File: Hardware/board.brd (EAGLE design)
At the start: 106.4 x 75.2 mm, 105 parts, among them IC1 BQ25180YBGR, IC2 DRV2605YZFR, IC3 BMA423, IC9 RT6160AWSC, J1 503480-2400, J2 TC2030-IDC_TC2030-IDC, J4 KH-TYPE-C-16P, Q1 SI1308EDL-T1-GE3, Q2 3.1A/30V/105mΩ, U1 NRF52840_QF, U3 MAX17048G+T10, X1 32MHz, X2 32.768kHz

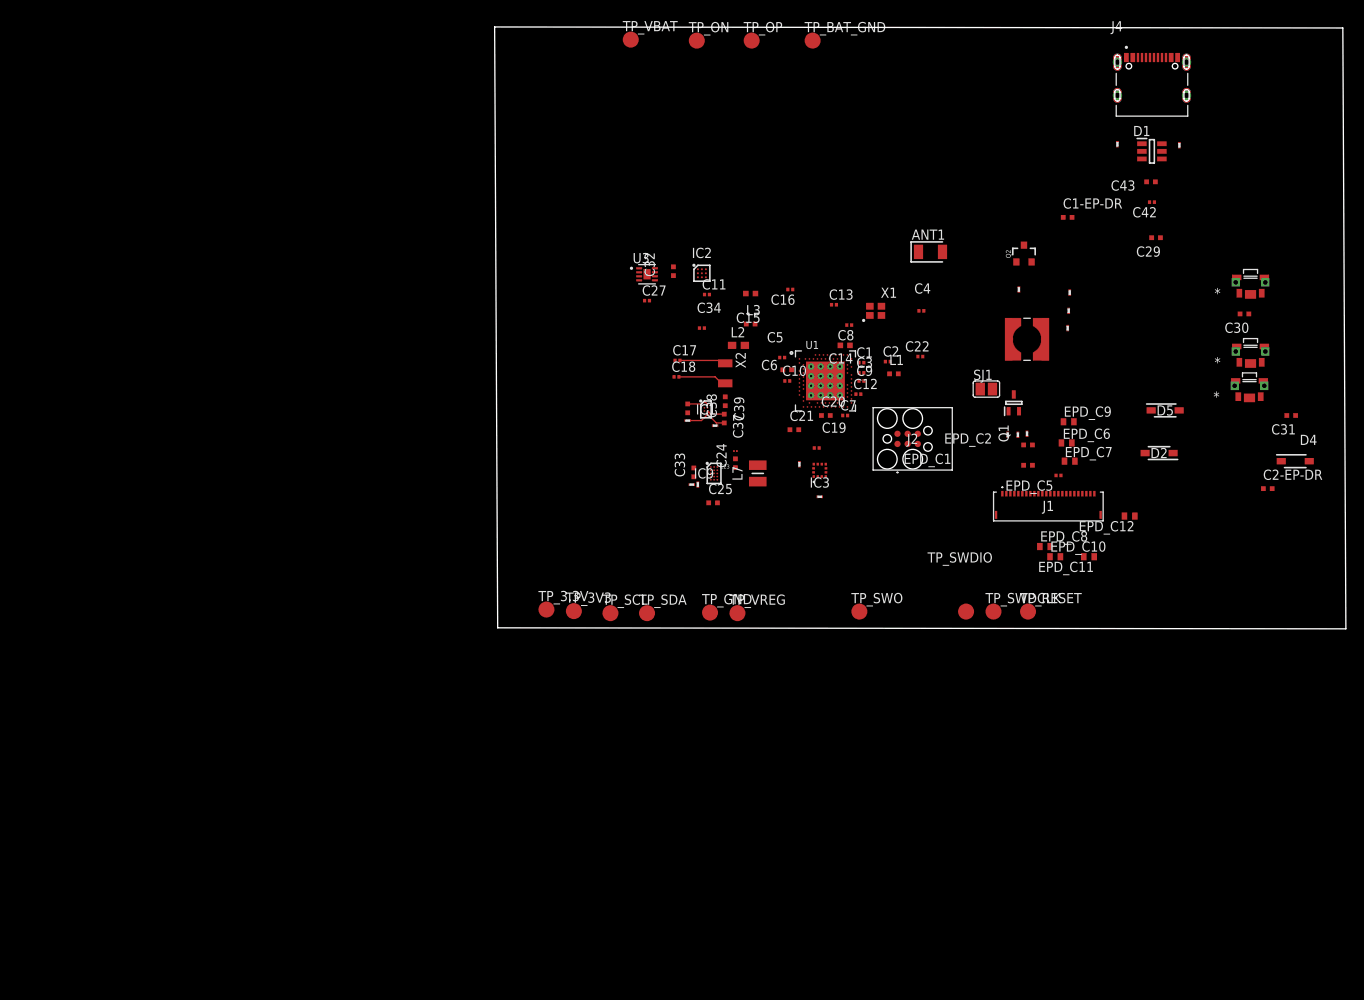
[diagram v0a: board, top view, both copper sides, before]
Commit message: Schematic and 2D PCB updated to final version
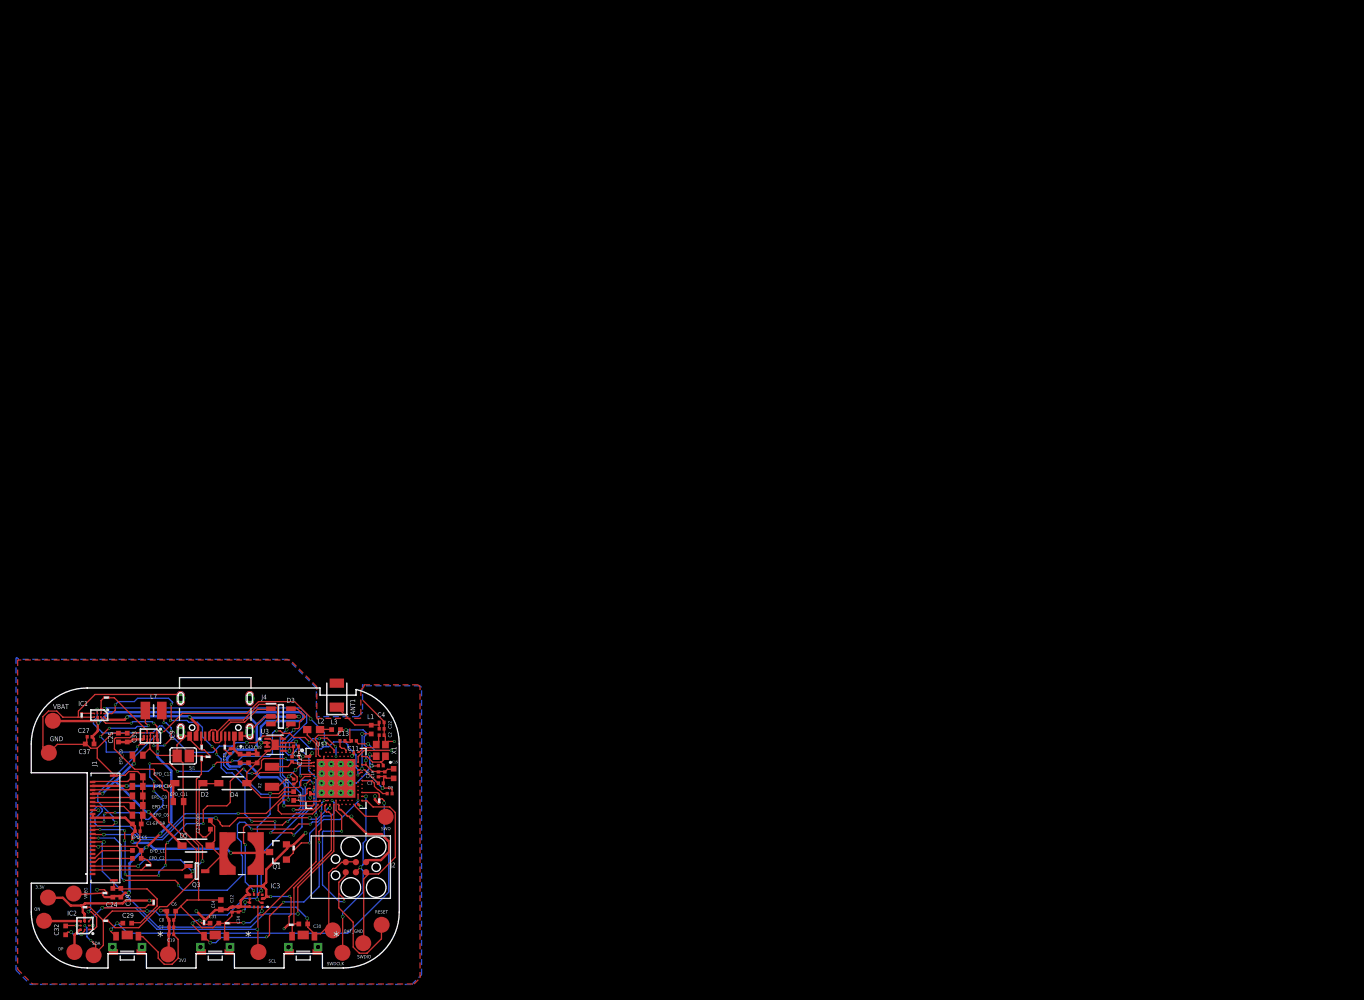
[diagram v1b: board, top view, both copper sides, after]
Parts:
- removed D1: ESP32_C6_LIBRARY_3_USBLC6-2SC6Y, InkTime_v5:ESP32_C6_LIBRARY_3_SOT95P280X145-6N
- removed Q2: 3.1A/30V/105mΩ, InkTime_v5:ESP32_C6_LIBRARY_4_ESP32_C6_LIBRARY_4_ESP32_C6_LIBRARY_4_ESP32_C6_LIBRARY_4_ESP32_WROVER_SPARKFUN-DISCRETESE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
- removed TP_3.3V, TP_3V3, TP_BAT_GND, TP_GND, TP_ON, TP_OP, TP_RESET, TP_SCL, TP_SDA, TP_SWDCLK, TP_SWDIO, TP_SWO, TP_VBAT, TP_VREG: HECTOR_WATCH_1_TPTP20R, InkTime_v5:HECTOR_WATCH_1_TP20R
- removed U1: NRF52840_QF, InkTime_v5:NORDIC_NRF_4_AQFN50P700X700X85_HS-74N
- added 3.3V, 3V3, BAT_GND, GND, ON, OP, RESET, SCL, SDA, SWDCLK, SWDIO, SWO, VBAT, VREG: HECTOR_WATCH_1_TPTP20R, InkTime_v5:HECTOR_WATCH_1_TP20R
- added D3: ESP32_C6_LIBRARY_3_USBLC6-2SC6Y, InkTime_v5:ESP32_C6_LIBRARY_3_SOT95P280X145-6N
- added Q3: SI1308EDL-T1-GE3, InkTime_v5:ESP32_C6_LIBRARY_6_SOT65P210X110-3N
- added U$1: NORDIC_NRF_4_NRF52840_QF, InkTime_v5:NORDIC_NRF_4_AQFN50P700X700X85_HS-74N
- C23: device InkTime_v5:GRM011R60J152KE01L_2_CAPC0201X13N -> InkTime_v5:GRM011R60J152KE01L_1_0201
- Q1: value SI1308EDL-T1-GE3 -> 3.1A/30V/105mΩ; device InkTime_v5:ESP32_C6_LIBRARY_6_SOT65P210X110-3N -> InkTime_v5:ESP32_C6_LIBRARY_4_ESP32_C6_LIBRARY_4_ESP32_C6_LIBRARY_4_ESP32_C6_LIBRARY_4_ESP32_WROVER_SPARKFUN-DISCRETESE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
- moved SW_DN 162.8 mm to (-11.0, -14.5), turned to 180 degrees
- moved C29 154.5 mm to (-11.0, -11.9), turned to 0 degrees
- moved C31 148.8 mm to (-0.10, -11.9), turned to 0 degrees
- moved SW_ENT 146.7 mm to (0.00, -14.5), turned to 180 degrees
- moved R2_USB 143.5 mm to (-1.70, 10.1)
- moved C30 140.2 mm to (11.0, -12.0), turned to 0 degrees
- moved SW_UP 139.5 mm to (11.0, -14.5), turned to 180 degrees
- moved J4 139.3 mm to (0.00, 16.2), turned to 180 degrees
- moved C1-EP-DR 138.9 mm to (-9.80, 0.50)
- moved D4 138.8 mm to (2.20, 5.60), turned to 180 degrees
- moved C2-EP-DR 138.7 mm to (-0.60, 0.40), turned to 90 degrees
- moved R1_USB 134.6 mm to (1.20, 10.1), turned to 180 degrees
- moved C42 134.1 mm to (1.90, 9.60), turned to 270 degrees
- moved C43 133.9 mm to (4.17, 8.70), turned to 270 degrees
- moved D5 132.8 mm to (-2.40, -2.20)
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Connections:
- net N$9 renamed 3.3V
- removed net 3V3/1.7D: C34.1, IC2.C2, Q2.2, R5.2, R7.2, R8.2, R_PWR_EPD.2
- removed net 3V3/2.4A: C12.1, C14.1, C19.1, C6.1, C7.1, C8.1, IC3.10, IC3.3, IC3.7, J2.1, R17.1, R18.1, TP_3.3V.TP, TP_3V3.TP, U1.P$A22, U1.P$AD14, U1.P$AD23, U1.P$B1, U1.P$W1, U1.P$Y2
- removed net ALERT/1.6C: U3.5
- removed net ALERT/2.5C: U1.P$J24
- removed net D+/1.5D: D1.4
- removed net D+/2.7D: U1.P$AD6
- removed net D-/1.5D: D1.6
- removed net D-/2.7D: U1.P$AD4
- removed net EPD_BUSY/1.5D: J1.9
- removed net EPD_BUSY/2.2D: U1.P$AD12
- removed net EPD_CS/1.4C: J1.12
- removed net EPD_CS/2.2D: U1.P$K2
- removed net EPD_DC/1.5D: J1.11
- removed net EPD_DC/2.2D: U1.P$AD10
- removed net EPD_RST/1.5D: J1.10
- removed net EPD_RST/2.2D: U1.P$AC11
- removed net HAPTIC_EN/1.4C: IC2.A1
- removed net HAPTIC_EN/2.6A: U1.P$U1
- removed net MOSI/1.5B: J1.14
- removed net MOSI/2.2D: U1.P$B13
- removed net P0.13/1.5D: C30.1, R5.1, SW_UP.2
- removed net P0.13/2.6C: U1.P$AD8
- removed net P0.14/1.5D: C31.1, R8.1, SW_ENT.2
- removed net P0.14/2.7C: U1.P$AC9
- removed net P1.01/1.6C: Q2.1, R_PWR_EPD.1
- removed net P1.01/2.4B: U1.P$Y23
- removed net P1.02/1.6C: C29.1, R7.1, SW_DN.2
- removed net P1.02/2.8C: U1.P$W24
- removed net SCK/1.5B: J1.13
- removed net SCK/2.2D: U1.P$A12
- removed net SCL/1.4C: IC2.C1, U3.7
- removed net SCL/2.4C: IC1.B1, IC3.12, R17.2, R4.1, TP_SCL.TP, U1.P$M2
- removed net SDA/1.4C: IC2.B2, U3.8
- removed net SDA/2.4C: IC1.C1, IC3.2, R1.1, R18.2, TP_SDA.TP, U1.P$L1
- removed net VBAT/1.2A: C27.1, TP_VBAT.TP, U3.2, U3.3
- removed net VBAT/2.5C: C37.1, IC1.C2
- removed net VBUS/1.5D: C42.1, C43.1, D1.5, J4.A4_B9, J4.A9_B4
- removed net VBUS/2.6D: C21.1, C38.1, IC1.A2, U1.P$AD2
- new net 3V3: 3.3V.TP, 3V3.TP, C12.1, C14.1, C19.1, C34.1, C6.1, C7.1, C8.1, IC2.C2, IC3.10, IC3.3, IC3.7, J2.1, Q1.2, R17.1, R18.1, R5.2, R7.2, R8.2, R_PWR_EPD.2, U$1.P$A22, U$1.P$AD14, U$1.P$AD23, U$1.P$B1, U$1.P$W1, U$1.P$Y2
- new net ALERT: U$1.P$J24, U3.5
- new net D+: D3.4, U$1.P$AD6
- new net D-: D3.6, U$1.P$AD4
- new net EPD_BUSY: J1.9, U$1.P$AD12
- new net EPD_CS: J1.12, U$1.P$K2
- new net EPD_DC: J1.11, U$1.P$AD10
- new net EPD_RST: J1.10, U$1.P$AC11
- new net HAPTIC_EN: IC2.A1, U$1.P$U1
- new net MOSI: J1.14, U$1.P$B13
- new net P0.13: C30.1, R5.1, SW_UP.2, U$1.P$AD8
- new net P0.14: C31.1, R8.1, SW_ENT.2, U$1.P$AC9
- new net P1.01: Q1.1, R_PWR_EPD.1, U$1.P$Y23
- new net P1.02: C29.1, R7.1, SW_DN.2, U$1.P$W24
- new net SCK: J1.13, U$1.P$A12
- new net SCL: IC1.B1, IC2.C1, IC3.12, R17.2, R4.1, SCL.TP, U$1.P$M2, U3.7
- new net SDA: IC1.C1, IC2.B2, IC3.2, R1.1, R18.2, SDA.TP, U$1.P$L1, U3.8
- new net VBAT: C27.1, C37.1, IC1.C2, U3.2, U3.3, VBAT.TP
- new net VBUS: C21.1, C38.1, C42.1, C43.1, D3.5, IC1.A2, J4.A4_B9, J4.A9_B4, U$1.P$AD2
- net DEC3: now also U$1.P$D23; no longer U1.P$D23
- net DEC4_6: now also U$1.P$B5, U$1.P$E24; no longer U1.P$B5, U1.P$E24
- net DN: now also D3.1; no longer D1.1
- net DP: now also D3.3; no longer D1.3
- net EPD_3V3: now also Q1.3; no longer Q2.3
- net GDR: now also Q3.1; no longer Q1.1
- net GND: now also BAT_GND.TP, C23.1, D3.2, GND.TP, U$1.P$74, U$1.P$75, U$1.P$76, U$1.P$77, U$1.P$78, U$1.P$79, U$1.P$80, U$1.P$81, U$1.P$82, U$1.P$83, U$1.P$84, U$1.P$85, U$1.P$86, U$1.P$87, U$1.P$88, U$1.P$89, U$1.P$90, U$1.P$B7, U$1.P$F23; no longer C23.2, D1.2, TP_BAT_GND.TP, TP_GND.TP, U1.P$74, U1.P$75, U1.P$76, U1.P$77, U1.P$78, U1.P$79, U1.P$80, U1.P$81, U1.P$82, U1.P$83, U1.P$84, U1.P$85, U1.P$86, U1.P$87, U1.P$88, U1.P$89, U1.P$90, U1.P$B7, U1.P$F23
- net IMU_INT1: now also U$1.P$N1; no longer U1.P$N1
- net IMU_INT2: now also U$1.P$P2; no longer U1.P$P2
- net N$1: now also U$1.P$C1; no longer U1.P$C1
- net N$12: now also U$1.P$A18; no longer U1.P$A18
- net N$13: now also U$1.P$A23; no longer U1.P$A23
- net N$14: now also U$1.P$B24; no longer U1.P$B24
- net N$16: now also U$1.P$H23; no longer U1.P$H23
- net N$17: now also Q3.3; no longer Q1.3
- net N$19: now also U$1.P$N24; no longer U1.P$N24
- net N$2: now also U$1.P$D2; no longer U1.P$D2
- net N$4: now also U$1.P$F2; no longer U1.P$F2
- net N$5: now also U$1.P$B3; no longer U1.P$B3
- net N$7: now also U$1.P$AC5; no longer U1.P$AC5
- net OUT+: now also OP.TP; no longer TP_OP.TP
- net OUT-: now also ON.TP; no longer TP_ON.TP
- net P0.04: now also U$1.P$J1; no longer U1.P$J1
- net P0.09: now also U$1.P$L24; no longer U1.P$L24
- net P0.19: now also U$1.P$AC15; no longer U1.P$AC15
- net P0.20: now also U$1.P$AD16; no longer U1.P$AD16
- net P0.21: now also U$1.P$AC17; no longer U1.P$AC17
- net P0.22: now also U$1.P$AD18; no longer U1.P$AD18
- net P0.23: now also U$1.P$AC19; no longer U1.P$AC19
- net P0.24: now also U$1.P$AD20; no longer U1.P$AD20
- net P0.25: now also U$1.P$AC21; no longer U1.P$AC21
- net P0.26: now also U$1.P$G1; no longer U1.P$G1
- net P0.27: now also U$1.P$H2; no longer U1.P$H2
- net P0.28: now also U$1.P$B11; no longer U1.P$B11
- net P0.29: now also U$1.P$A10; no longer U1.P$A10
- net P0.30: now also U$1.P$B9; no longer U1.P$B9
- net P0.31: now also U$1.P$A8; no longer U1.P$A8
- net P1.03: now also U$1.P$V23; no longer U1.P$V23
- net P1.04: now also U$1.P$U24; no longer U1.P$U24
- net P1.05: now also U$1.P$T23; no longer U1.P$T23
- net P1.06: now also U$1.P$R24; no longer U1.P$R24
- net P1.07: now also U$1.P$P23; no longer U1.P$P23
- net P1.09: now also U$1.P$R1; no longer U1.P$R1
- net P1.10: now also U$1.P$A20; no longer U1.P$A20
- net P1.11: now also U$1.P$B19; no longer U1.P$B19
- net P1.12: now also U$1.P$B17; no longer U1.P$B17
- net P1.13: now also U$1.P$A16; no longer U1.P$A16
- net P1.14: now also U$1.P$B15; no longer U1.P$B15
- net P1.15: now also U$1.P$A14; no longer U1.P$A14
- net PMIC_INT: now also U$1.P$T2; no longer U1.P$T2
- net RESE: now also Q3.2; no longer Q1.2
- net RESET: now also RESET.TP, U$1.P$AC13; no longer TP_RESET.TP, U1.P$AC13
- net SWDCLK: now also SWDCLK.TP, U$1.P$AA24; no longer TP_SWDCLK.TP, U1.P$AA24
- net SWDIO: now also SWDIO.TP, U$1.P$AC24; no longer TP_SWDIO.TP, U1.P$AC24
- net SWO: now also SWO.TP, U$1.P$AD22; no longer TP_SWO.TP, U1.P$AD22
- net VREG: now also C23.2, VREG.TP; no longer C23.1, TP_VREG.TP
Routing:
- net GND: track 5.10 -> 243.2 mm, vias 0 -> 12
- net SCL: track 0.00 -> 99.6 mm, vias 0 -> 7
- net SDA: track 0.00 -> 93.1 mm, vias 0 -> 7
- net 3V3: track 0.00 -> 73.6 mm, vias 0 -> 14
- net VBUS: track 0.00 -> 58.6 mm, vias 0 -> 5
- net P1.02: track 0.00 -> 54.7 mm, vias 0 -> 3
- net HAPTIC_EN: track 0.00 -> 50.6 mm, vias 0 -> 2
- net EPD_BUSY: track 0.00 -> 48.8 mm, vias 0 -> 2
- net MOSI: track 0.00 -> 46.5 mm, vias 0 -> 14
- net EPD_CS: track 0.00 -> 46.4 mm, vias 0 -> 12
- net EPD_RST: track 0.00 -> 46.4 mm, vias 0 -> 6
- net PMIC_INT: track 0.00 -> 46.3 mm, vias 0 -> 10
- net SCK: track 0.00 -> 45.6 mm, vias 0 -> 4
- net VBAT: track 0.00 -> 45.2 mm, vias 0 -> 2
- net N$8: track 0.00 -> 41.1 mm
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- added copper zone on layer 15, net 3V3
- added copper zone on layer 1, net GND
- added copper zone on layer 16, net GND
- added copper zone on layer 2, net GND
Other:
- board size 106.4 x 75.2 mm -> 46 x 35 mm
